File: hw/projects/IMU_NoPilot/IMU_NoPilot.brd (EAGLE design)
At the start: 30 x 42 mm, 43 parts, among them P1 USB_MICRO_AB, P2 ST_LINK, P3 PWR3, U1 STM32F4XX_64, U2 LSM303DLHC, U3 LSM330DLC, U4 MPL3115A2, U5 MTK-3329, U6 MCP1825

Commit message: -
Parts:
- moved C13 5.05 mm to (14.2, 6.50), turned to 0 degrees
- moved C15 2.88 mm to (15.2, 3.50), turned to 270 degrees
- moved C14 1.64 mm to (13.2, 3.50), turned to 270 degrees
- moved U3 0.70 mm to (14.2, 4.00), turned to 90 degrees
- turned C8 to 180 degrees
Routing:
- net GND: track 0.00 -> 98.1 mm, vias 0 -> 22
- net VDD: track 0.00 -> 53.7 mm, vias 0 -> 15
- net VDD_5: track 0.00 -> 26.4 mm, vias 0 -> 2
- net DP: track 0.00 -> 15.2 mm
- net DM: track 0.00 -> 14.2 mm
- added copper zone on layer 2, net GND
- added copper zone on layer 3, net VDD

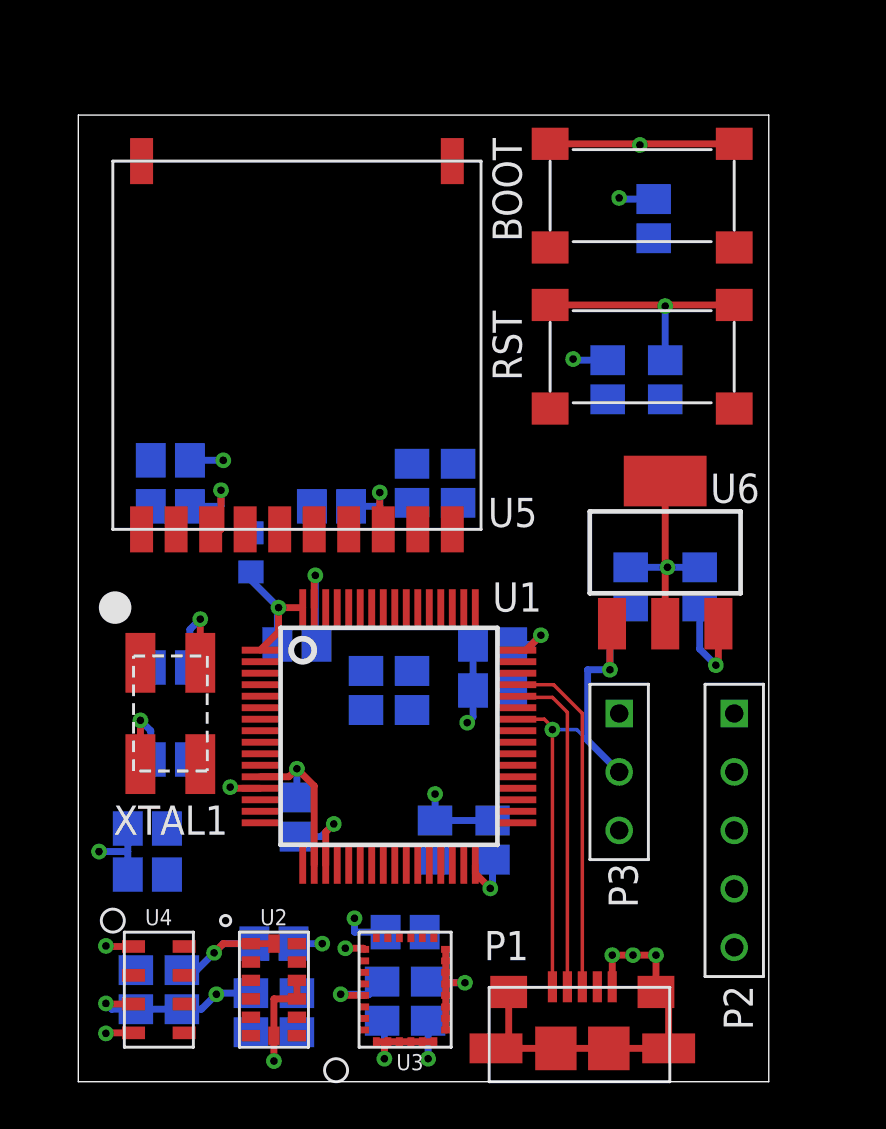
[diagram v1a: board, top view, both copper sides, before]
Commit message: some manual power routing and some small adjustments to placement
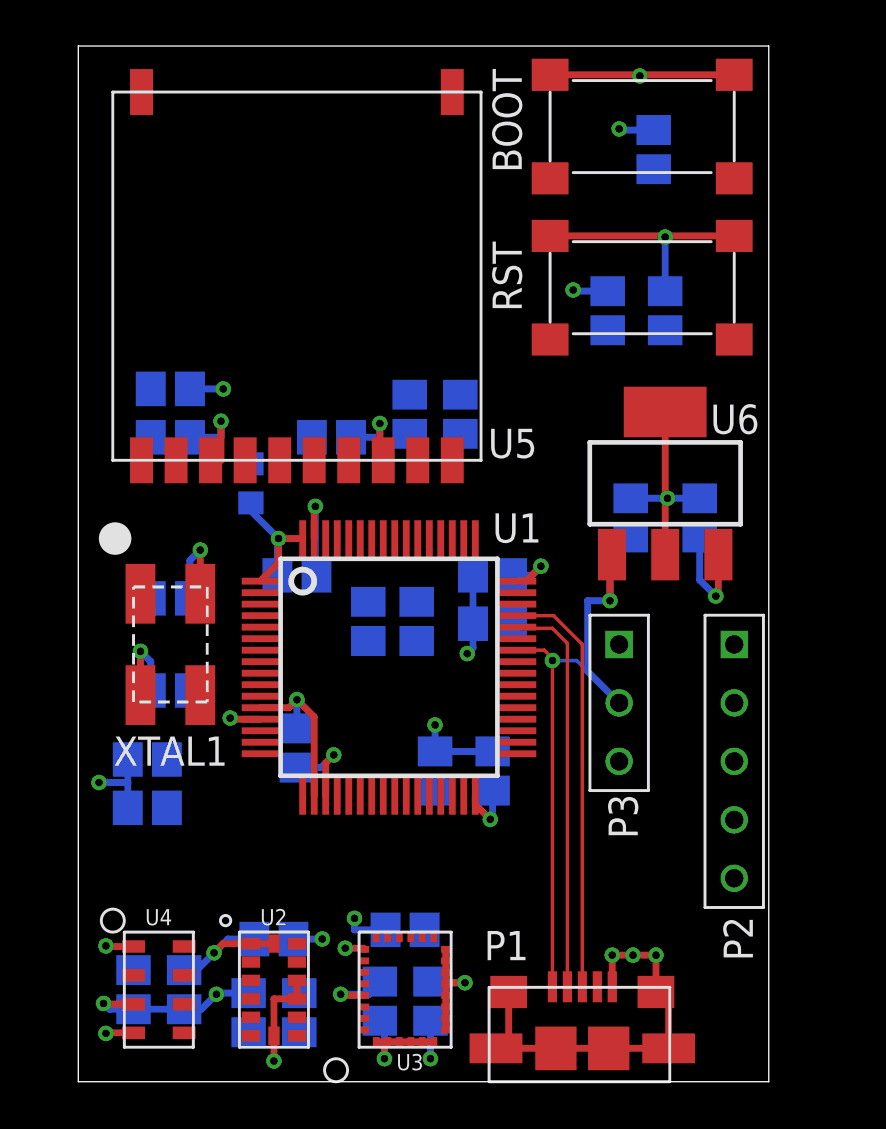
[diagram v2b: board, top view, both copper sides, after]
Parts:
- moved C19 3.10 mm to (4.00, 30.1)
- moved R5 3.01 mm to (14.7, 20.0)
- moved R3 3.00 mm to (14.4, 29.0)
- moved R4 3.00 mm to (16.6, 29.0)
- moved R6 3.00 mm to (12.6, 20.0)
- moved BOOT 3.00 mm to (24.5, 41.5)
- moved C18 3.00 mm to (11.0, 28.0)
- moved C2 3.00 mm to (15.5, 13.5)
- moved C20 3.00 mm to (4.00, 28.0)
- moved C21 3.00 mm to (24.0, 24.5)
- moved C22 3.00 mm to (27.0, 24.5)
- moved C3 3.00 mm to (9.50, 14.5)
- moved C4 3.00 mm to (9.50, 22.0)
- moved C5 3.00 mm to (18.0, 13.5)
- moved C6 3.00 mm to (18.0, 22.0)
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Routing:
- net VDD_5: track 26.4 -> 29.4 mm
- net DP: track 15.2 -> 18.2 mm
- net DM: track 14.2 -> 17.2 mm
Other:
- board size 30 x 42 mm -> 30 x 45 mm

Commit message: -
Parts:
- moved C13 4.02 mm to (17.8, 8.40), turned to 180 degrees
- moved C14 1.98 mm to (11.7, 2.10)
- moved C15 1.66 mm to (16.8, 2.80)
- moved U3 0.50 mm to (14.2, 4.50)
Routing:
- net N$10: track 0.00 -> 3.14 mm, vias 0 -> 1
- net VDD: track 53.7 -> 52.5 mm, vias 15 -> 13
- net GND: track 98.2 -> 98.0 mm, vias 22 -> 23

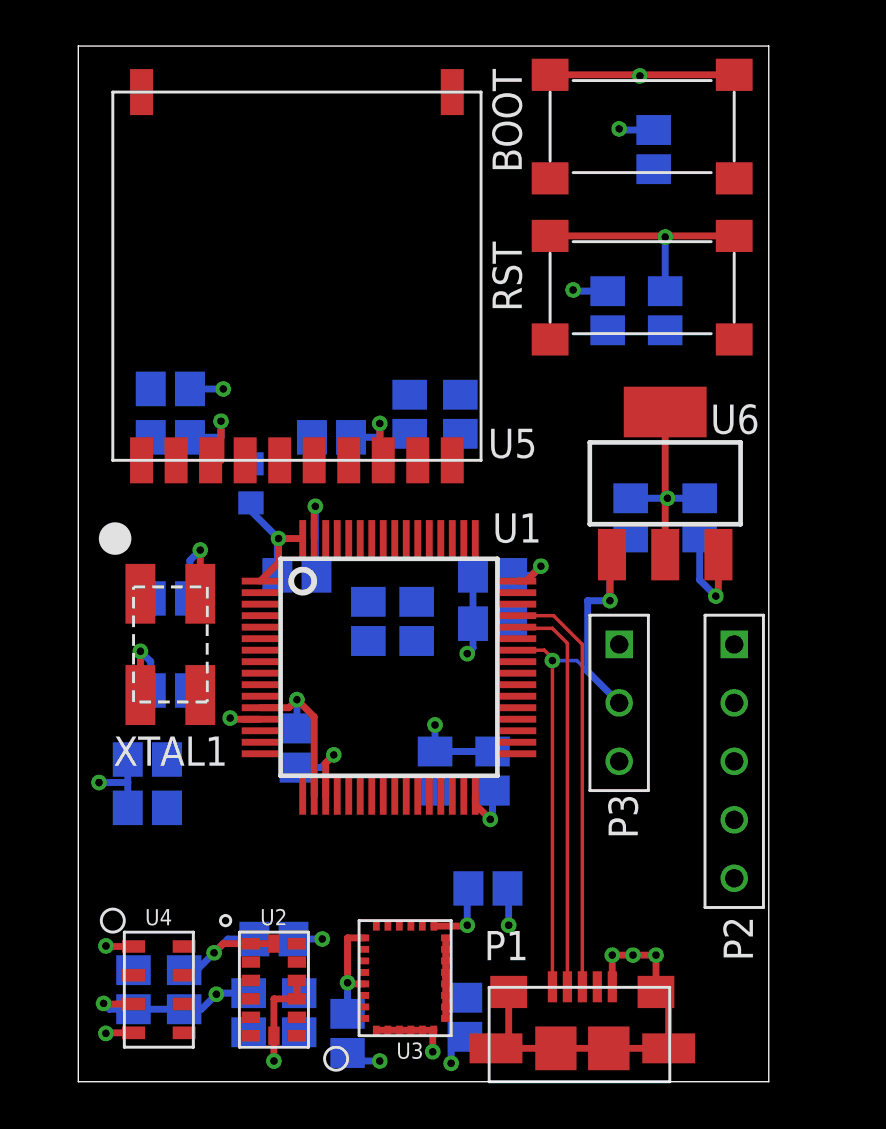
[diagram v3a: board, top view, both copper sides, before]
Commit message: Changed all small caps, and all res to 0402. Large caps are 0805. Ripped all routing to start over again
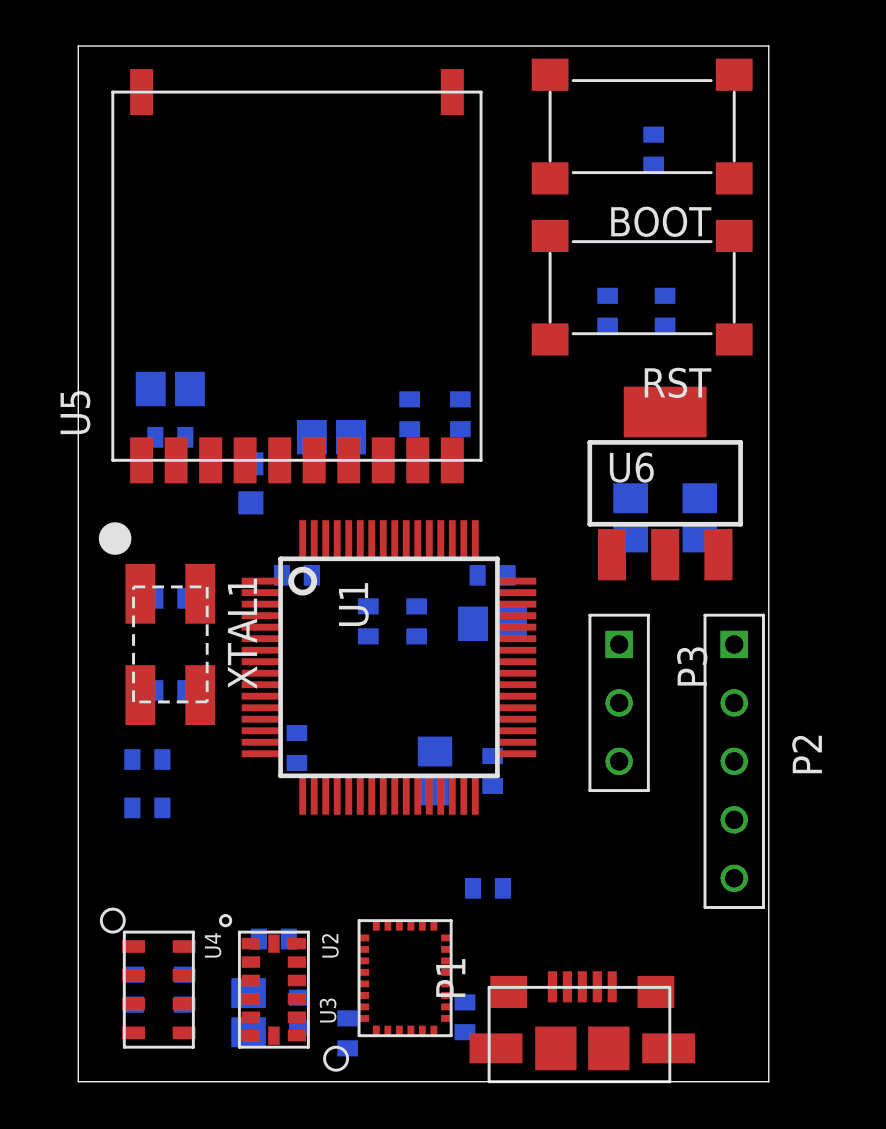
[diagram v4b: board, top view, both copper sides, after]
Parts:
- C11, C12, C13, C14, C15, C16, C17, C20, C3, C4, C5, C6, C7, C8, C9: device resistor:C0805 -> resistor:C0402
- R1, R2, R3, R4, R5, R6, R7, R8: device resistor:R0805 -> resistor:R0402
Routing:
- net GND: track 98.0 -> 0.00 mm, vias 23 -> 0
- net VDD: track 52.5 -> 0.00 mm, vias 13 -> 0
- net VDD_5: track 29.4 -> 0.00 mm, vias 2 -> 0
- net DP: track 18.2 -> 0.00 mm
- net DM: track 17.2 -> 0.00 mm
- net N$10: track 3.14 -> 0.00 mm, vias 1 -> 0

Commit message: Cleanup of power and layout
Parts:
- added P4: SPI_EXT, connectors:PINLIST5_2P54
- moved L1 7.44 mm to (3.70, 32.4), turned to 0 degrees
- moved P3 6.12 mm to (28.4, 22.6), flipped to the bottom, turned to 270 degrees
- moved C22 5.44 mm to (24.9, 29.5), turned to 0 degrees
- moved U6 2.94 mm to (23.4, 28.0), turned to 90 degrees
- moved R5 2.90 mm to (11.8, 20.0)
- moved R4 2.62 mm to (16.3, 26.4)
- moved R3 2.62 mm to (14.7, 26.4)
- moved P1 2.50 mm to (24.4, 4.80)
- moved C17 2.32 mm to (2.35, 4.55)
- moved C12 2.30 mm to (9.50, 5.30)
- moved C3 2.28 mm to (8.40, 12.5), turned to 270 degrees
- moved C21 2.17 mm to (24.9, 26.5), turned to 0 degrees
- moved C5 2.04 mm to (17.6, 11.5), turned to 270 degrees
- moved C2 1.92 mm to (17.2, 14.4), turned to 0 degrees
- moved R6 1.90 mm to (10.7, 20.0)
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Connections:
- new net SPIEXT_CLK: P4.P$1, U1.34
- new net SPIEXT_MISO: P4.P$3, U1.35
- new net SPIEXT_MOSI: P4.P$2, U1.36
- new net SPIEXT_NSS: P4.P$4, U1.33
- net GND: now also P4.P$5
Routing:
- net GND: track 0.00 -> 111.6 mm, vias 0 -> 38
- net VDD: track 0.00 -> 59.1 mm, vias 0 -> 16
- net VDD_5: track 0.00 -> 39.6 mm, vias 0 -> 5
- net DP: track 0.00 -> 21.4 mm
- net DM: track 0.00 -> 20.3 mm
- net !RST: track 0.00 -> 12.8 mm, vias 0 -> 1
- net BOOT: track 0.00 -> 9.95 mm, vias 0 -> 1
- net VDD_GPS: track 0.00 -> 7.05 mm, vias 0 -> 1
- net N$11: track 0.00 -> 2.43 mm, vias 0 -> 1

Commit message: -
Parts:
- moved C7 0.67 mm to (4.30, 17.6)
- moved C8 0.67 mm to (4.30, 21.6)
- moved XTAL1 0.67 mm to (4.30, 19.6)
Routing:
- net N$4: track 0.00 -> 9.45 mm, vias 0 -> 1
- net N$6: track 0.00 -> 7.05 mm, vias 0 -> 1
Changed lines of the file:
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@@
 <element name="C5" library="resistor" package="C0402" value="100n" x="17.6" y="11.5" rot="MR270"/>
 <element name="C6" library="resistor" package="C0402" value="100n" x="18.6" y="22" rot="MR0"/>
-<element name="XTAL1" library="misc_devices" package="XTAL_5X3P2" value="XTAL_5X3P2" x="4" y="19" rot="R270"/>
-<element name="C8" library="resistor" package="C0402" value="" x="4" y="21" rot="MR180"/>
-<element name="C7" library="resistor" package="C0402" value="" x="4" y="17" rot="MR0"/>
+<element name="XTAL1" library="misc_devices" package="XTAL_5X3P2" value="XTAL_5X3P2" x="4.3" y="19.6" rot="R270"/>
+<element name="C8" library="resistor" package="C0402" value="" x="4.3" y="21.6" rot="MR180"/>
+<element name="C7" library="resistor" package="C0402" value="" x="4.3" y="17.6" rot="MR0"/>
 <element name="RST" library="misc_devices" package="OMROM_B3FS-1XXX" value="OMRON_B3FS_1000" x="24.5" y="35.25" rot="R180"/>
 <element name="BOOT" library="misc_devices" package="OMROM_B3FS-1XXX" value="OMRON_B3FS_1000" x="24.5" y="41.5" rot="R180"/>
@@
 <wire x1="4.2" y1="28.6" x2="4.15" y2="28.6" width="0.5" layer="16"/>
 <wire x1="4.15" y1="28.6" x2="4.15" y2="27" width="0.5" layer="16"/>
-<wire x1="5.3" y1="21.2" x2="4" y2="21.2" width="0.3" layer="1"/>
-<wire x1="4" y1="21.2" x2="4" y2="22.1" width="0.3" layer="1"/>
-<via x="4" y="22.1" extent="1-16" drill="0.3302"/>
-<wire x1="4.65" y1="21" x2="4.65" y2="22.1" width="0.3" layer="16"/>
-<wire x1="4.65" y1="22.1" x2="4" y2="22.1" width="0.3" layer="16"/>
-<wire x1="2.7" y1="16.8" x2="4" y2="16.8" width="0.3" layer="1"/>
-<wire x1="4" y1="16.8" x2="4" y2="15.95" width="0.3" layer="1"/>
-<via x="4" y="15.95" extent="1-16" drill="0.3302"/>
-<wire x1="3.35" y1="17" x2="3.35" y2="15.95" width="0.3" layer="16"/>
-<wire x1="3.35" y1="15.95" x2="4" y2="15.95" width="0.3" layer="16"/>
+<wire x1="5.6" y1="21.8" x2="4.3" y2="21.8" width="0.3" layer="1"/>
+<wire x1="4.3" y1="21.8" x2="4.3" y2="22.7" width="0.3" layer="1"/>
+<via x="4.3" y="22.7" extent="1-16" drill="0.3302"/>
+<wire x1="4.95" y1="21.6" x2="4.95" y2="22.7" width="0.3" layer="16"/>
+<wire x1="4.95" y1="22.7" x2="4.3" y2="22.7" width="0.3" layer="16"/>
+<wire x1="3" y1="17.4" x2="4.3" y2="17.4" width="0.3" layer="1"/>
+<wire x1="4.3" y1="17.4" x2="4.3" y2="16.55" width="0.3" layer="1"/>
+<via x="4.3" y="16.55" extent="1-16" drill="0.3302"/>
+<wire x1="3.65" y1="17.6" x2="3.65" y2="16.55" width="0.3" layer="16"/>
+<wire x1="3.65" y1="16.55" x2="4.3" y2="16.55" width="0.3" layer="16"/>
 <wire x1="8.7" y1="21.55" x2="8.7" y2="21.75" width="0.3" layer="16"/>
 <wire x1="8.7" y1="21.75" x2="9.75" y2="21.75" width="0.3" layer="16"/>
@@
 <contactref element="XTAL1" pad="P$1"/>
 <contactref element="U1" pad="5"/>
-<wire x1="3.35" y1="21" x2="7.9" y2="19.75" width="0" layer="19" extent="1-16"/>
-<wire x1="2.7" y1="21.2" x2="3.35" y2="21" width="0" layer="19" extent="1-16"/>
+<wire x1="3" y1="19.75" x2="3" y2="21.8" width="0.1524" layer="1"/>
+<wire x1="3.65" y1="21.6" x2="4.3" y2="21.6" width="0.1524" layer="16"/>
+<wire x1="4.3" y1="21.6" x2="4.3" y2="19.75" width="0.1524" layer="16"/>
+<via x="4.3" y="19.75" extent="1-16" drill="0.3302"/>
+<wire x1="3" y1="19.75" x2="4.3" y2="19.75" width="0.1524" layer="1"/>
+<wire x1="4.3" y1="19.75" x2="7.9" y2="19.75" width="0.1524" layer="1"/>
 </signal>
 <signal name="N$6">
@@
 <contactref element="XTAL1" pad="P$3"/>
 <contactref element="U1" pad="6"/>
-<wire x1="5.3" y1="16.8" x2="7.9" y2="19.25" width="0" layer="19" extent="1-1"/>
-<wire x1="4.65" y1="17" x2="5.3" y2="16.8" width="0" layer="19" extent="1-16"/>
+<wire x1="7.9" y1="19.25" x2="5.6" y2="19.25" width="0.1524" layer="1"/>
+<wire x1="5.6" y1="19.25" x2="5.6" y2="18.65" width="0.1524" layer="1"/>
+<wire x1="5.6" y1="18.6" x2="5.6" y2="17.4" width="0.1524" layer="1"/>
+<wire x1="4.95" y1="17.6" x2="4.95" y2="18.65" width="0.1524" layer="16"/>
+<wire x1="4.95" y1="18.65" x2="4.35" y2="18.65" width="0.1524" layer="16"/>
+<via x="4.35" y="18.65" extent="1-16" drill="0.3302"/>
+<wire x1="5.6" y1="18.6" x2="5.6" y2="18.65" width="0.1524" layer="1"/>
+<wire x1="5.6" y1="18.65" x2="4.35" y2="18.65" width="0.1524" layer="1"/>
 </signal>
 <signal name="BOOT">
@@
 <wire x1="23.35" y1="7.2" x2="24.4" y2="7.2" width="0.1524" layer="1"/>
 <wire x1="24.4" y1="7.2" x2="24.4" y2="4.1" width="0.1524" layer="1"/>
-<wire x1="24.4" y1="4.1" x2="24.4" y2="4.125" width="0" layer="19" extent="1-16"/>
+<wire x1="24.4" y1="4.1" x2="24.4" y2="4.125" width="0" layer="19" extent="1-1"/>
 </signal>
 <signal name="SWDIO">

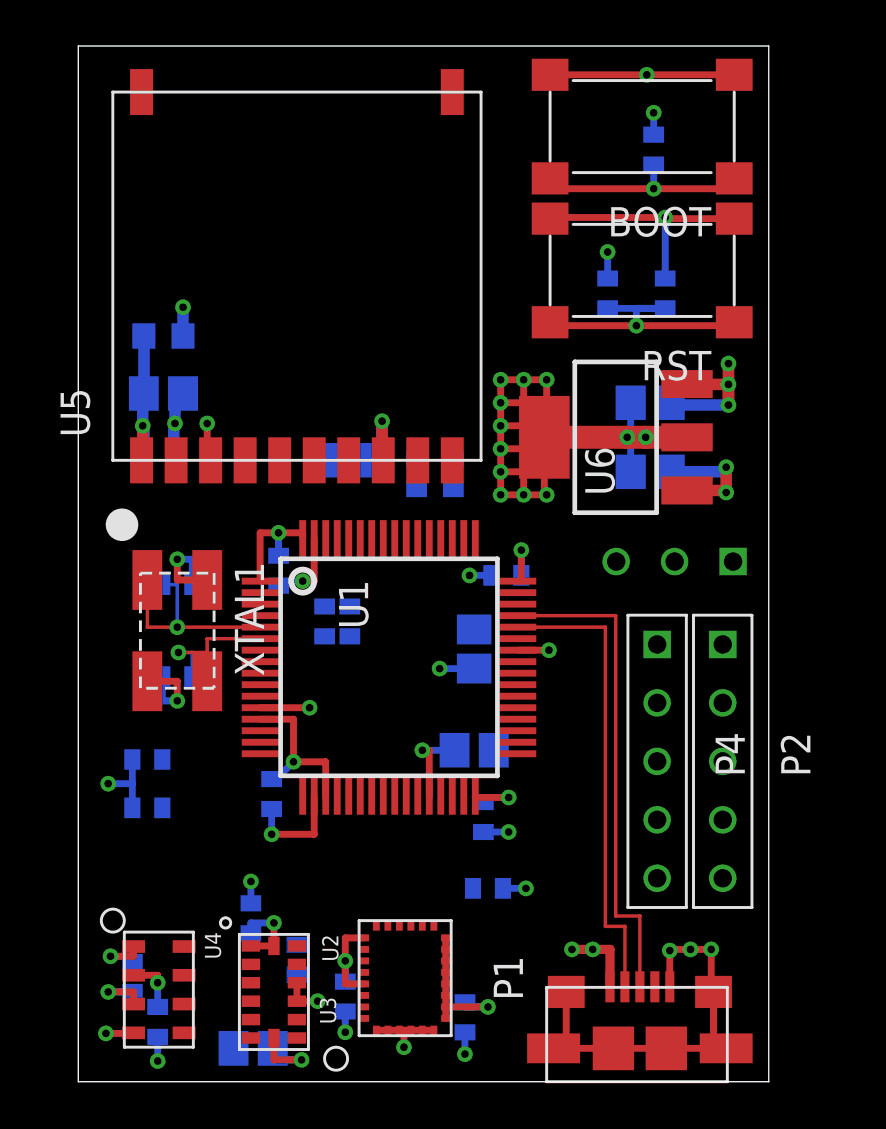
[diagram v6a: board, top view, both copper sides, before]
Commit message: Fixed silk screen
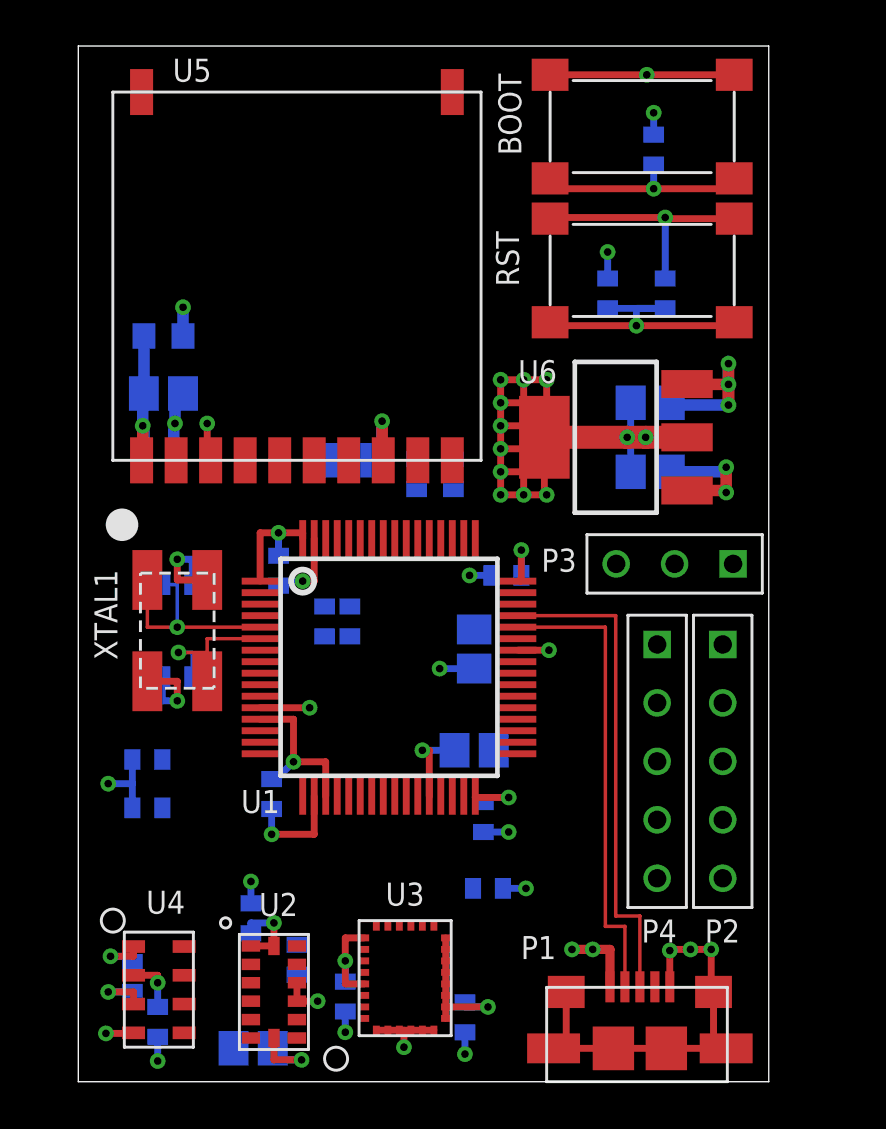
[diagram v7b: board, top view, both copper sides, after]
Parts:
- moved P3 0.10 mm to (28.4, 22.5), flipped to the top, turned to 90 degrees
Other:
- board text added: "(c) 2012 Kjell H Andersen"
- board text added: "IMU NoPilot"
- board text added: "http://code.google.com/p/nopilot/"
